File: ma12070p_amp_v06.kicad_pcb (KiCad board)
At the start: 2 copper layers, 100.4 x 80.4 mm, 85 parts, among them U1 MAX16956AUBD/V+, U2 MA12070P

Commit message: minor changes
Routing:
- net OUT1B: track 34.8 -> 33.0 mm
- net OUT1A: track 24.3 -> 22.6 mm
- net OUT0B: track 44.0 -> 42.3 mm
- net OUT0A: track 27.6 -> 25.9 mm
- net Net-(C45-Pad1): track 48.4 -> 47.7 mm
- net Net-(C41-Pad1): track 9.82 -> 9.23 mm
- net Net-(C46-Pad2): track 24.4 -> 23.8 mm
- net Net-(C14-Pad2): track 11.0 -> 10.5 mm
- net VDD: track 190.2 -> 190.0 mm, vias 4 -> 3
- net GND: vias 190 -> 201

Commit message: filename cleanup
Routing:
- net VDD: track 190.0 -> 186.5 mm
- net Ext_supply_5V: track 21.5 -> 24.9 mm
- net Net-(C44-Pad1): track 24.7 -> 25.3 mm
- net GND: vias 201 -> 204

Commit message: cleanup
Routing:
- net CLKMS: track 29.8 -> 28.4 mm
- net SDA: track 39.4 -> 38.7 mm
- net Net-(C25-Pad2): track 10.3 -> 10.9 mm
- net ENABLE: track 47.2 -> 47.7 mm
- net GND: vias 204 -> 216

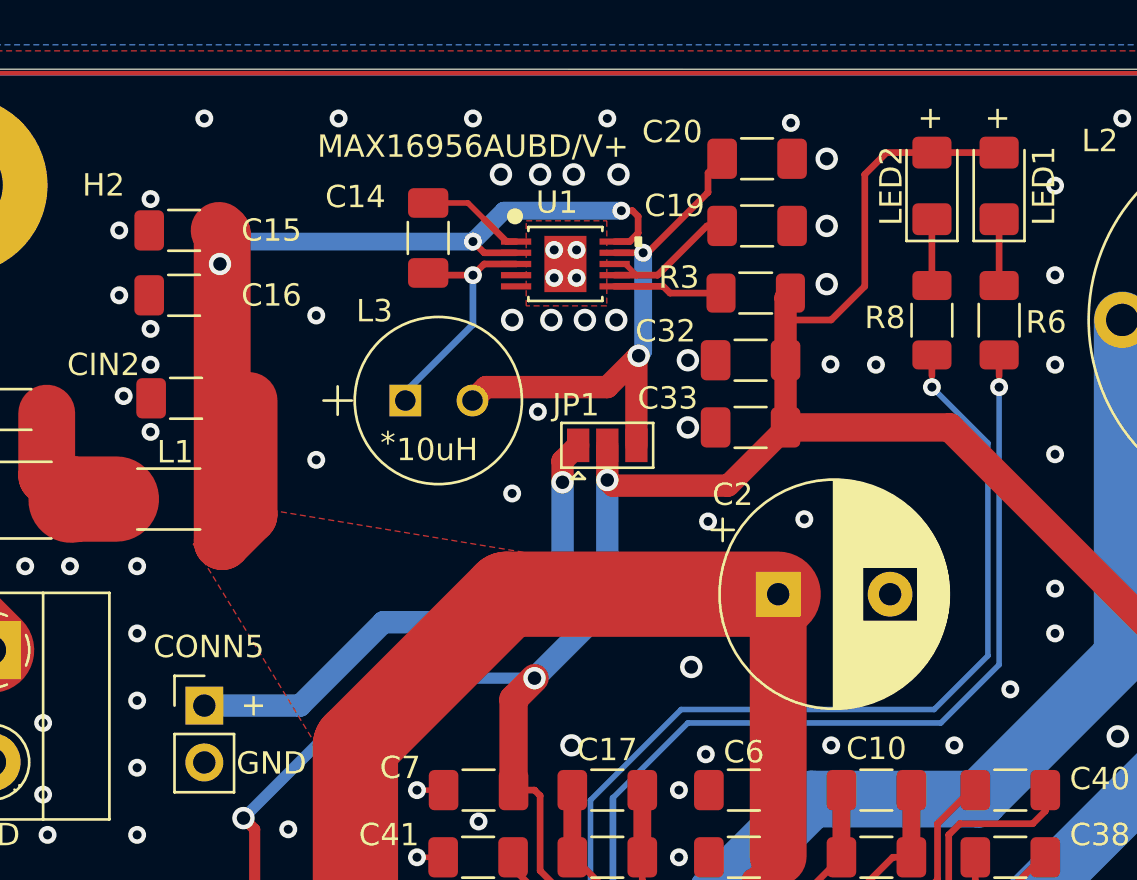
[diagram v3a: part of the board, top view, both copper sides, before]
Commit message: updated dcdc  converter
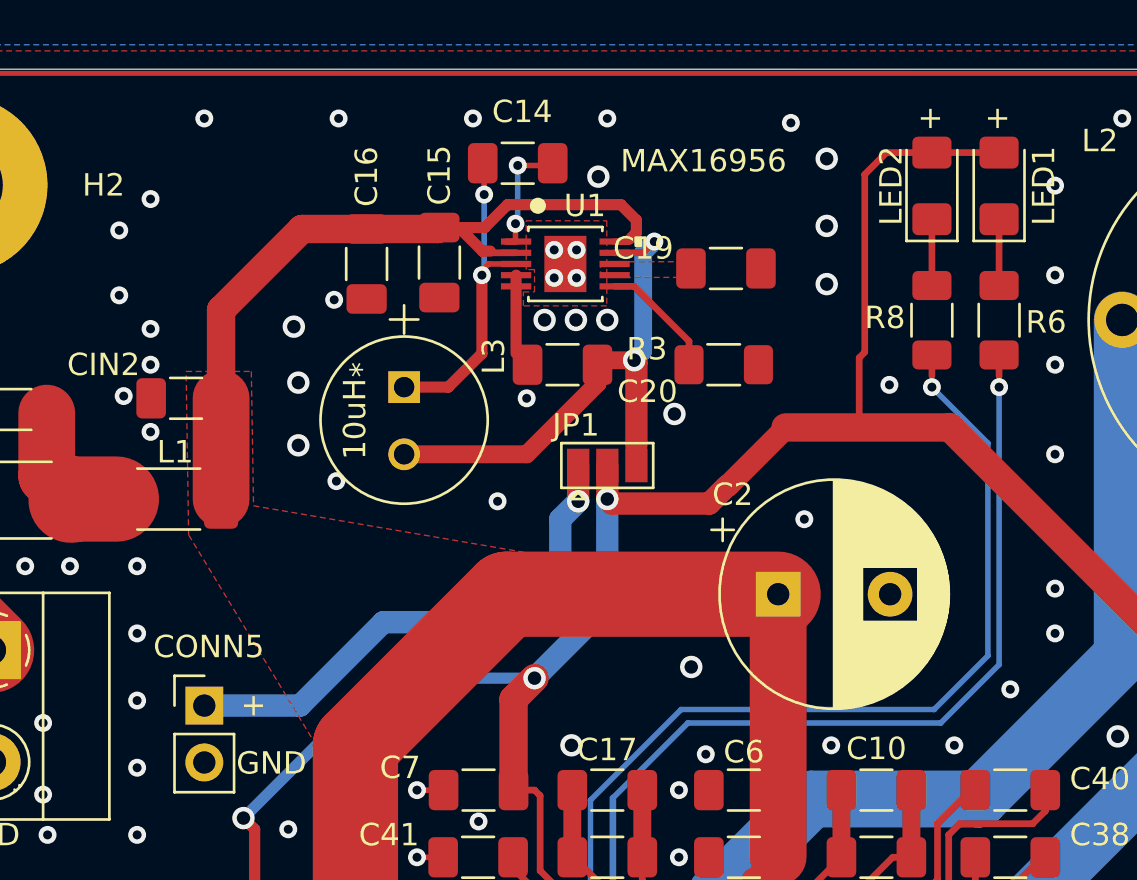
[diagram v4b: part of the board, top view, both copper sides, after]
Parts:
- removed C32, C33: 10uF, Capacitor_SMD:C_1206_3216Metric_Pad1.33x1.80mm_HandSolder
- U1: value MAX16956AUBD/V+ -> MAX16956
- moved C20 12.7 mm to (142.0, 57.0), turned to 180 degrees
- moved C15 11.5 mm to (136.5, 52.4), turned to -90 degrees
- moved C16 8.27 mm to (133.2, 52.5), turned to -90 degrees
- moved C14 5.21 mm to (140.0, 48.0), turned to 180 degrees
- moved R3 3.50 mm to (149.2, 57.0)
- moved C19 2.35 mm to (149.3, 52.7)
- moved L3 1.77 mm to (135.0, 59.5), turned to -90 degrees
- moved JP1 0.90 mm to (144.0, 61.5)
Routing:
- net PVDD: track 164.5 -> 148.0 mm, vias 3 -> 0
- net Net-(C19-Pad1): track 6.42 -> 0.42 mm
- net GND: track 8.27 -> 12.5 mm, vias 216 -> 212
- net Net-(C14-Pad2): track 10.5 -> 14.7 mm, vias 1 -> 2
- net VDD: track 186.9 -> 182.8 mm
- net Ext_supply_5V: track 24.9 -> 24.0 mm
- net Net-(C14-Pad1): track 4.64 -> 5.48 mm, vias 0 -> 2
- net Net-(R3-Pad2): track 4.87 -> 5.39 mm
- added copper zone on F.Cu, net Net-(C19-Pad1)

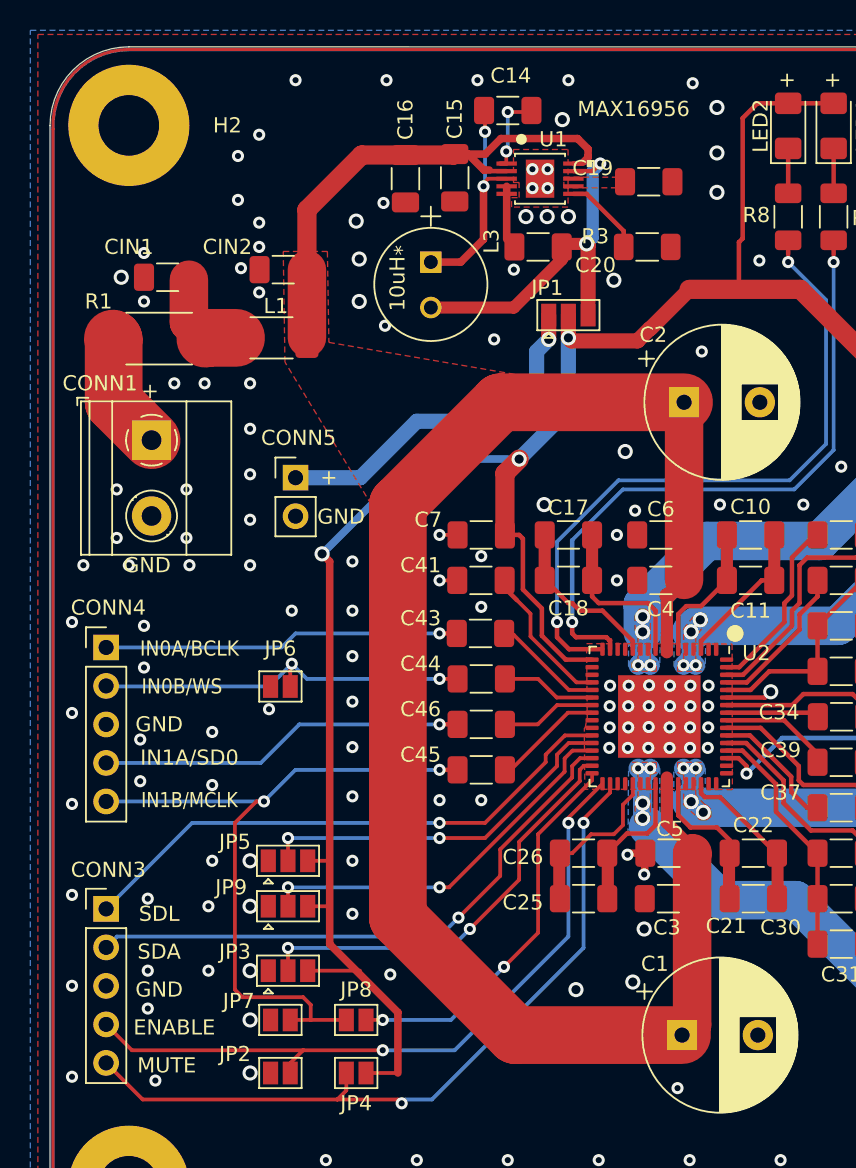
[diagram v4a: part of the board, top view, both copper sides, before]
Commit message: miror improvements and calculation voltage regulator
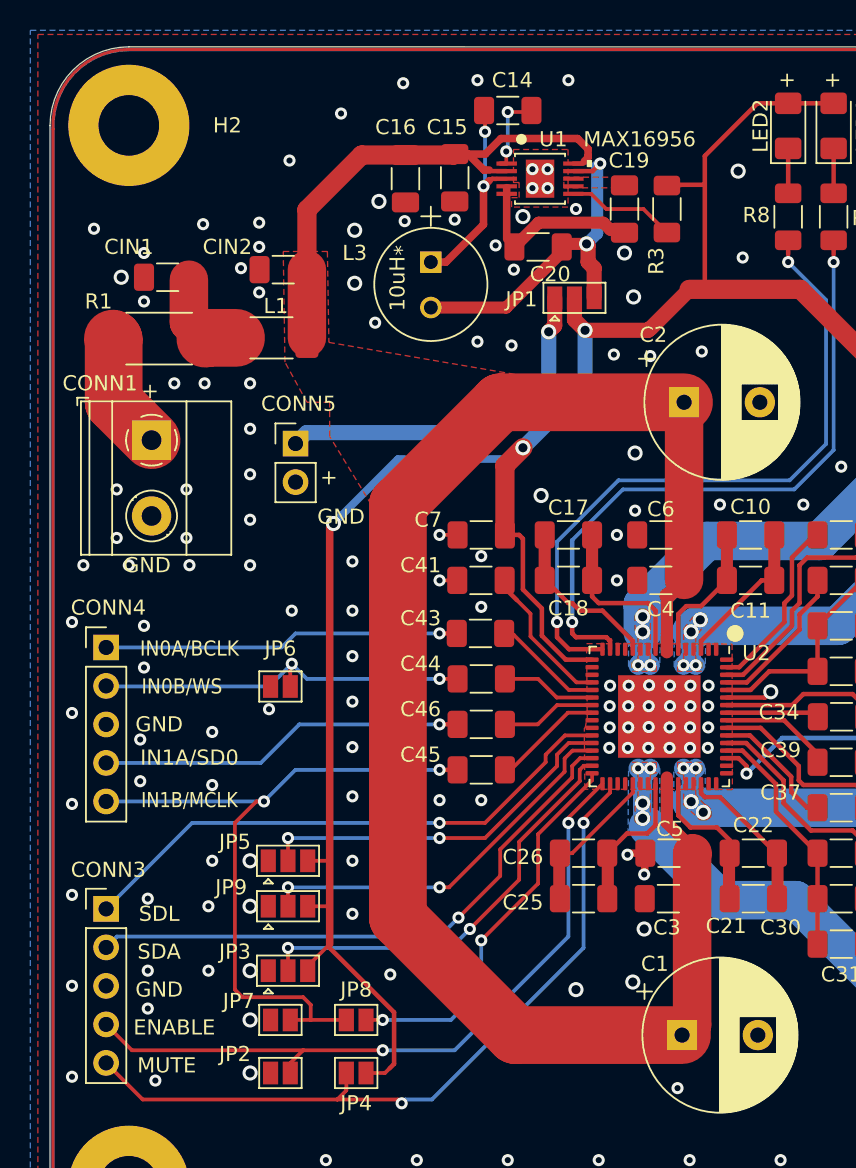
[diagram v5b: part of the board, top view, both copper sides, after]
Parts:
- moved R3 2.82 mm to (150.5, 54.5), turned to -90 degrees
- moved C19 2.41 mm to (147.7, 54.5), turned to -90 degrees
- moved CONN5 2.25 mm to (126.0, 70.0)
- moved JP1 1.21 mm to (144.4, 60.4)
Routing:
- net GND: track 12.5 -> 20.5 mm, vias 212 -> 213
- net VDD: track 182.8 -> 185.1 mm
- net Net-(R3-Pad2): track 5.39 -> 7.23 mm
- net Net-(C25-Pad2): track 10.9 -> 10.1 mm

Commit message: minor change
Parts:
- moved L6 0.50 mm to (174.0, 113.0)
- moved L2 0.25 mm to (174.0, 55.2)
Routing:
- net OUT1B: track 33.0 -> 32.2 mm
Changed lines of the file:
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@@
   )
   (footprint "Inductor_Murata_TH:L_Radial_TH_Murata_D16.9_P14.0" (layer "F.Cu")
-    (at 174 55 180)
+    (at 174 55.25 180)
     (property "Sheetfile" "ma12070p_amp_v1.kicad_sch")
     (property "Sheetname" "")
@@
   )
   (footprint "Inductor_Murata_TH:L_Radial_TH_Murata_D16.9_P14.0" (layer "F.Cu")
-    (at 174.5 113 180)
+    (at 174 113 180)
     (property "Sheetfile" "ma12070p_amp_v1.kicad_sch")
     (property "Sheetname" "")
@@
   (segment (start 139.927497 53.500001) (end 139.927497 53.089211) (width 0.5) (layer "F.Cu") (net 1))
   (segment (start 136.6875 76) (end 135.5 76) (width 0.25) (layer "F.Cu") (net 1))
-  (segment (start 146.3 55.4) (end 142.0375 55.4) (width 0.8) (layer "F.Cu") (net 1))
-  (segment (start 142.0375 55.4) (end 140.4375 57) (width 0.8) (layer "F.Cu") (net 1))
+  (segment (start 145.8 55.2) (end 142.8 55.2) (width 0.8) (layer "F.Cu") (net 1))
   (segment (start 139.927497 53.500001) (end 139.927497 56.489997) (width 0.5) (layer "F.Cu") (net 1))
   (segment (start 149.0375 98.3625) (end 149 98.4) (width 0.5) (layer "F.Cu") (net 1))
+  (segment (start 142.8 55.2) (end 141 57) (width 0.8) (layer "F.Cu") (net 1))
+  (segment (start 141 57) (end 140.4375 57) (width 0.8) (layer "F.Cu") (net 1))
+  (segment (start 146.4625 55.8625) (end 145.8 55.2) (width 0.8) (layer "F.Cu") (net 1))
   (segment (start 149.0375 97) (end 148 97) (width 0.5) (layer "F.Cu") (net 1))
   (segment (start 154.4375 86.73) (end 156.97 86.73) (width 0.3) (layer "F.Cu") (net 1))
   (segment (start 149.0375 97) (end 149.0375 98.3625) (width 0.5) (layer "F.Cu") (net 1))
-  (segment (start 146.7625 55.8625) (end 146.3 55.4) (width 0.8) (layer "F.Cu") (net 1))
   (segment (start 135.5 79) (end 136.6675 79) (width 0.25) (layer "F.Cu") (net 1))
   (segment (start 156.97 86.73) (end 157.35 86.35) (width 0.3) (layer "F.Cu") (net 1))
-  (segment (start 147.7 55.8625) (end 146.7625 55.8625) (width 0.8) (layer "F.Cu") (net 1))
+  (segment (start 147.7 55.8625) (end 146.4625 55.8625) (width 0.8) (layer "F.Cu") (net 1))
   (segment (start 148 97) (end 147.9 97.1) (width 0.5) (layer "F.Cu") (net 1))
   (segment (start 157.5 86.25) (end 157.25 86.25) (width 0.3) (layer "F.Cu") (net 1))
@@
   (segment (start 148.9 91.9) (end 149.4 91.4) (width 1.27) (layer "B.Cu") (net 16))
   (segment (start 148.9 93.7) (end 148.9 94.9) (width 1.27) (layer "B.Cu") (net 16))
+  (segment (start 157.9 100.1) (end 167 109.2) (width 2.54) (layer "B.Cu") (net 16))
+  (segment (start 167 109.2) (end 167 113) (width 2.54) (layer "B.Cu") (net 16))
   (segment (start 148.9 93.7) (end 148.9 91.7) (width 1.27) (layer "B.Cu") (net 16))
   (segment (start 148.9 91.7) (end 148.6 91.4) (width 1.27) (layer "B.Cu") (net 16))
   (segment (start 149.25 95.25) (end 154.1 100.1) (width 2.54) (layer "B.Cu") (net 16))
   (segment (start 148.9 94.9) (end 149.25 95.25) (width 1.27) (layer "B.Cu") (net 16))
-  (segment (start 154.1 100.1) (end 159 100.1) (width 2.54) (layer "B.Cu") (net 16))
-  (segment (start 159 100.1) (end 167.5 108.6) (width 2.54) (layer "B.Cu") (net 16))
-  (segment (start 167.5 108.6) (end 167.5 113) (width 2.54) (layer "B.Cu") (net 16))
+  (segment (start 154.1 100.1) (end 157.9 100.1) (width 2.54) (layer "B.Cu") (net 16))
   (segment (start 193.95 100.55) (end 195.5 99) (width 2.54) (layer "F.Cu") (net 17))
   (segment (start 190 100.55) (end 193.95 100.55) (width 2.54) (layer "F.Cu") (net 17))
@@
   (segment (start 190 107.55) (end 190 112.5) (width 2.54) (layer "F.Cu") (net 51))
   (segment (start 190 112.5) (end 190.5 113) (width 2.54) (layer "F.Cu") (net 51))
-  (segment (start 181.5 111.232234) (end 188.282234 104.45) (width 2.54) (layer "F.Cu") (net 52))
-  (segment (start 181.5 113) (end 181.5 111.232234) (width 2.54) (layer "F.Cu") (net 52))
+  (segment (start 181 113) (end 181 111.732234) (width 2.54) (layer "F.Cu") (net 52))
   (segment (start 190 104.45) (end 193.95 104.45) (width 2.54) (layer "F.Cu") (net 52))
   (segment (start 195.5 105.1) (end 197.6 103) (width 2.54) (layer "F.Cu") (net 52))
   (segment (start 195.5 106) (end 195.5 105.1) (width 2.54) (layer "F.Cu") (net 52))
+  (segment (start 181 111.732234) (end 188.282234 104.45) (width 2.54) (layer "F.Cu") (net 52))
   (segment (start 202 103) (end 203.695 101.305) (width 2.54) (layer "F.Cu") (net 52))
   (segment (start 193.95 104.45) (end 195.5 106) (width 2.54) (layer "F.Cu") (net 52))
   (segment (start 197.6 103) (end 202 103) (width 2.54) (layer "F.Cu") (net 52))
-  (segment (start 188.282234 104.45) (end 190 104.45) (width 2.54) (layer "F.Cu") (net 52))
   (segment (start 203.695 101.305) (end 203.695 91.41) (width 2.54) (layer "F.Cu") (net 52))
+  (segment (start 188.282234 104.45) (end 190 104.45) (width 2.54) (layer "F.Cu") (net 52))
   (segment (start 154.4375 87.23) (end 158.77 87.23) (width 0.3) (layer "F.Cu") (net 53))
   (segment (start 158.77 87.23) (end 159.5 86.5) (width 0.3) (layer "F.Cu") (net 53))

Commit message: created gerber
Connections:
- C37 pad 1: VDD -> GND
- C42 pad 1: VDD -> GND
- C7 pad 1: VDD -> GND
- JP1 pad 2: VDD -> GND
- JP10 pad 3: VDD -> GND
- JP3 pad 3: VDD -> GND
- JP4 pad 1: VDD -> GND
- JP5 pad 3: VDD -> GND
- JP9 pad 3: VDD -> GND
- LED1 pad 2: VDD -> GND
- LED2 pad 2: VDD -> GND
- R3 pad 1: VDD -> GND
- U2 pad 17: VDD -> GND
- U2 pad 55: VDD -> GND
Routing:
- net VDD: track 185.1 -> 0.00 mm, vias 3 -> 0
- net GND: track 20.7 -> 205.6 mm, vias 213 -> 216
- net PVDD: track 147.9 -> 146.5 mm
- net ENABLE: track 47.7 -> 47.2 mm
